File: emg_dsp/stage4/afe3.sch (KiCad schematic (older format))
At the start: 57 parts, among them U32 8X2X100, U33 JUMP, U34 BAV199, U35 BAV199, U36 BAV199, U37 BAV199, U38 TLE2426, U39 REG101, U40 JUMP, U41 ISL28470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

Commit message: added the active electrode - just an INA, opamp, highpass and two lowpasses.
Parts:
- removed C67, C68, C69, C70, C73: 1uf, 0603, symbol C
- removed C71: 0.1uf, 0603, symbol C
- removed C72: 10nf, 0603, symbol C
- removed R26, R27, R28, R29, R30, R31, R32, R33: 2.2k, 0402, symbol R
- removed U32: 8X2X100, 2x8x100mil, symbol 8X2X100
- removed U33, U40: JUMP, 2x100mil, symbol JUMP
- removed U34, U35, U36, U37: BAV199, SOT-363, symbol BAV199
- removed U38: TLE2426, SOIC-8, symbol TLE2426
- removed U39: REG101, SOIC-8, symbol REG101
- removed U41: ISL28470, QSOP-28, symbol ISL28470
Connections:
- wire segments 217 -> 118
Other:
- note removed: "These diodes are optional"
- note removed: "as the inst. amp has ESD diodes"
- note removed: "if they are placed, need low leakage parts"

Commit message: notes, schematic mods, etc.
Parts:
- removed C143, C74, C75, C76, C78, C80, C81, C82: 4.7uf, 0603, symbol C
- removed C77, C79: 1uf, 0603, symbol C
- removed C83, C85, C86: 0.1uf, 0402, symbol C
- removed R34, R35, R41, R42: 327k, 0402, symbol R
- removed R36, R37, R39, R40: 3.3k, 0402, symbol R
- removed R38: 3.3k, 0603, symbol R
- removed U44: ZR4040-2.5, SOT-23, symbol ZR4040-5.0
- removed U45, U46: ADUM2400, SOICW-16, symbol ADUM2400
- added C? (x2): 22uf, 0805, symbol C
- added C? (x3): 10nf, 0402, symbol C
- added C? (x4): 10uf, 0603, symbol C
- added C? (x6): 1uf, 0402, symbol C
- added C? (x4): 1.5nf, 0402, symbol C
- added C? (x5): 2.2uf, 0402, symbol C
- added R? (x4): 1k, 0402, symbol R
- added R? (x5): 100k, 0402, symbol R
- added TP?: CH0, TP, symbol TP
- added TP?: CH1, TP, symbol TP
- added TP?: CH2, TP, symbol TP
- added TP?: CH3, TP, symbol TP
- added U?: MAX253, SOIC-8, symbol MAX253
- added U?: 78250, 78250M, symbol 78250M
- added U? (x6): BAT54S, SOT-23, symbol BAT54
- added U?: TPS78825, SOT-23-5, symbol TPS73025
- added U?: TPS72325, SOT-23-5, symbol TPS72301
- added U?: OPA4348, TSSOP-14, symbol OPA4348
- added U?: LP2985-50, SOT-23-5, symbol TPS73025
- added U? (x3): OPA4348, symbol OPA4348
- added U? (x2): IL715-3, SOIC-16, symbol ADUM2400
- D8: footprint SOD-323 -> SOD-523
- D9: value UCLAMP33 -> SOD-523
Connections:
- net labels added: AV+, AV-, AV0, AV5+, DIN, DOUT, V0, V5, _Enable
- net labels removed: AGnd, AVdd, Din, Dout, IN+A, IN+B, IN+C, IN+D, IN-A, IN-B, IN-C, IN-D, Vdd2
- wire segments 118 -> 173
- no-connect marks 0 -> 6
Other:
- note removed: "battery"
- note removed: "e.g. 4x AAA (6V)"
- note removed: "for loop stability"
- note removed: "may have to short the cap"
- note removed: "need to check this segment"
- moved on the sheet: C144, C84, D8, D9, L8, U42, U43

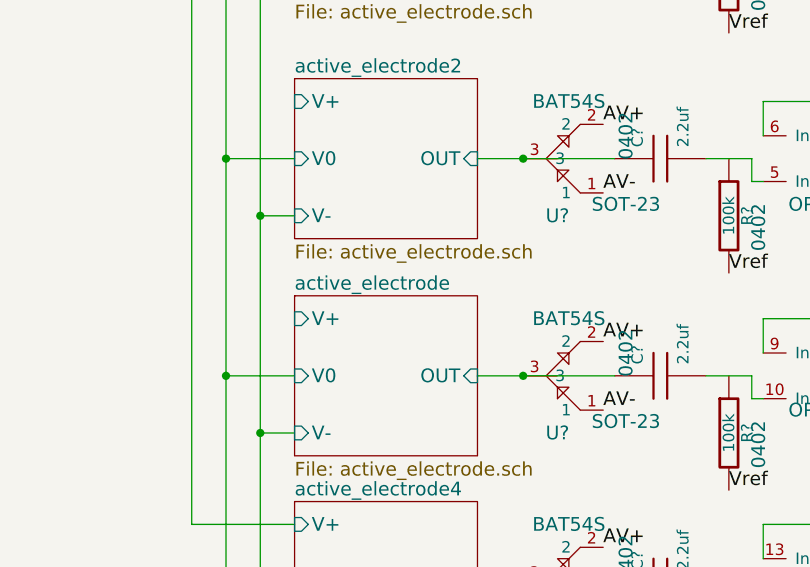
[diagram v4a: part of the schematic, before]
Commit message: revamping the neural AFE
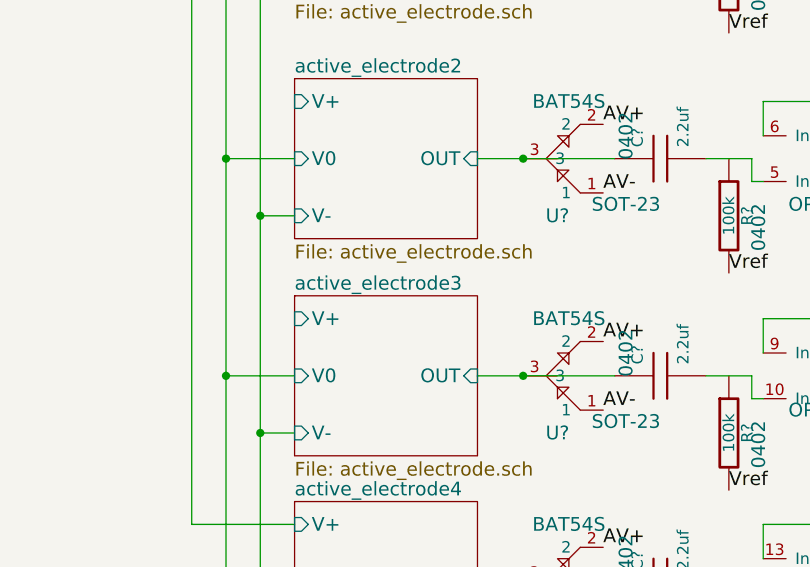
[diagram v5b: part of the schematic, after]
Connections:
- net active_electrode/OUT renamed active_electrode3/OUT
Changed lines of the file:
@@
-EESchema Schematic File Version 2  date Sun 31 Jan 2010 07:35:14 PM EST
+EESchema Schematic File Version 2  date Mon 01 Feb 2010 06:40:42 PM EST
 LIBS:power,device,emg_sym,./stage4.cache
 EELAYER 24  0
@@
 S 2550 3100 800  700
 U 4B6079F1
-F0 "active_electrode" 60
+F0 "active_electrode3" 60
 F1 "active_electrode.sch" 60
 F2 "OUT" I R 3350 3450 60

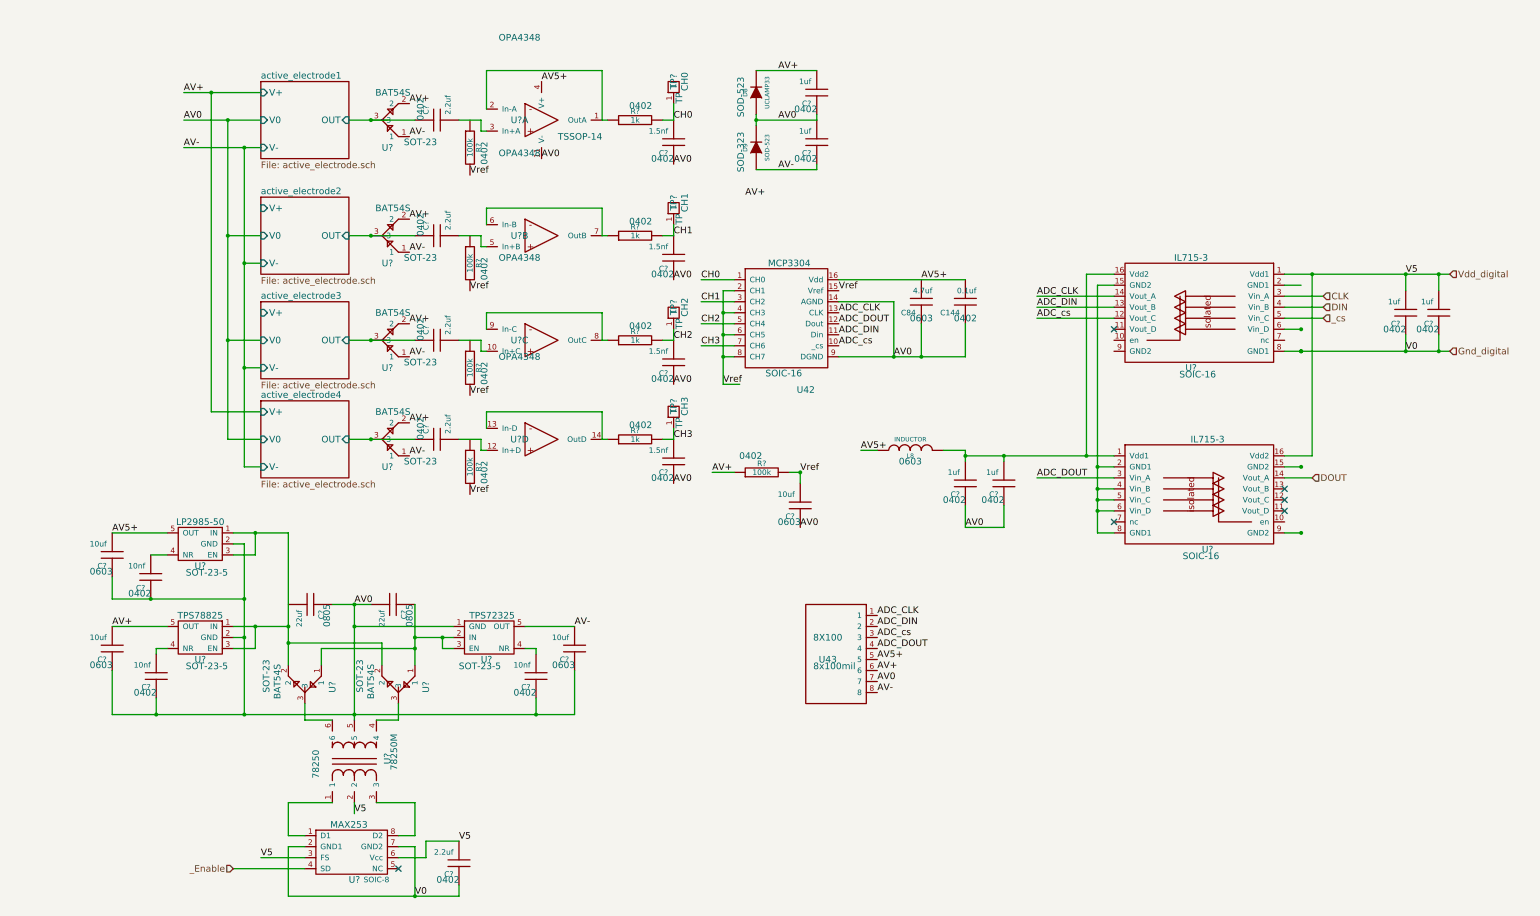
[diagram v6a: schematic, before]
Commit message: getting closer to finalizing the schematic ... added another voltage, beh.
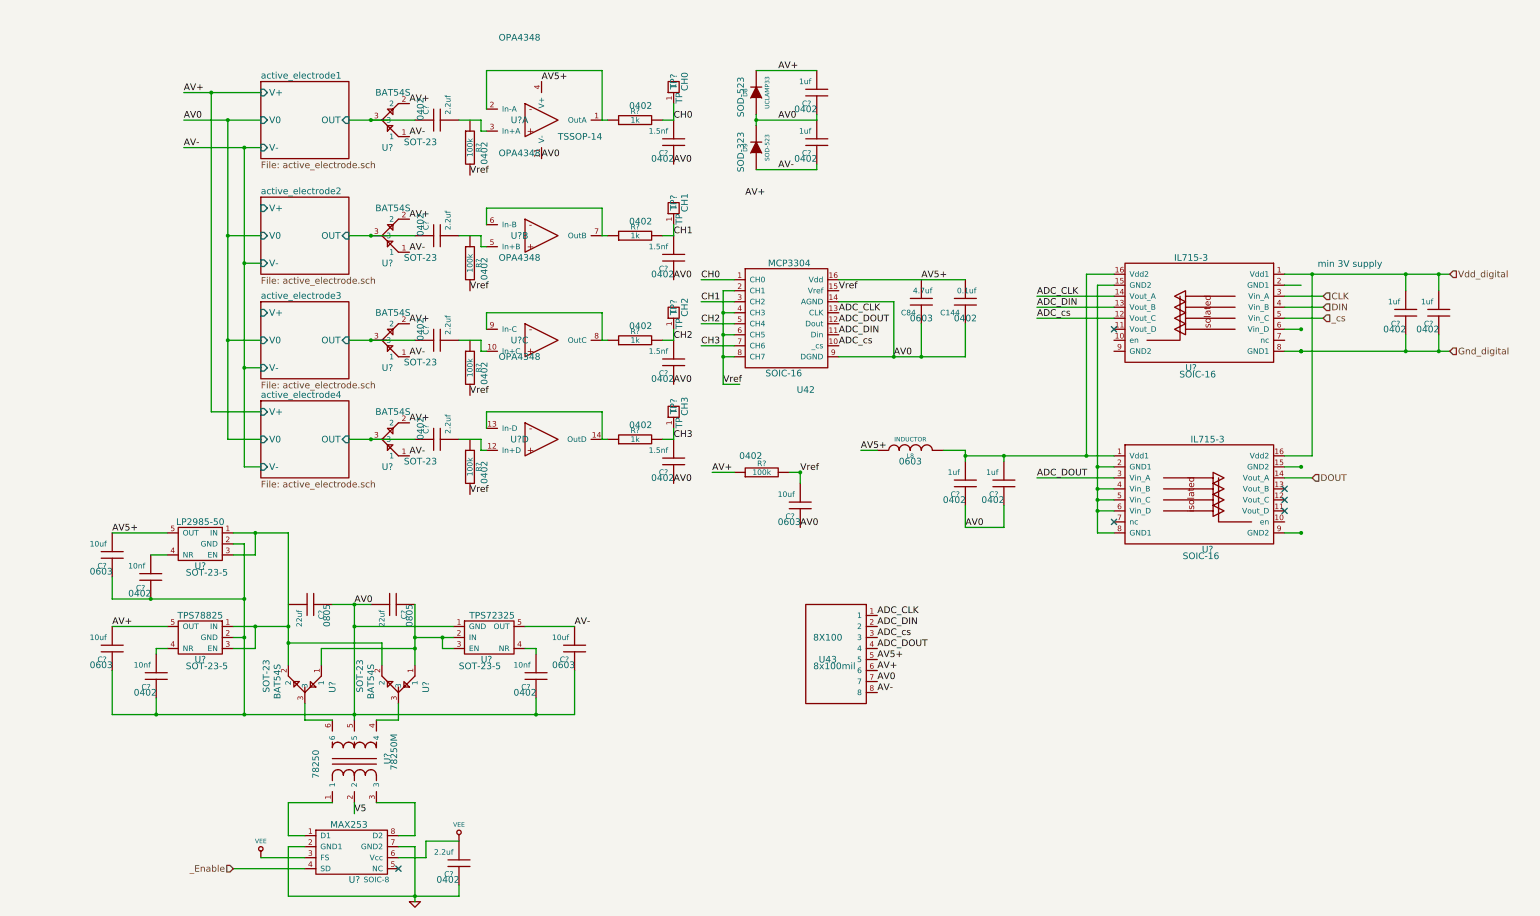
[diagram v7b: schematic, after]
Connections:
- net Gnd_digital: no longer C?.1, U?.2 (GND1), U?.7 (GND2)
- net Vdd_digital: no longer C?.2, U?.2, U?.3 (FS), U?.6 (Vcc)
- new net GND: C?.1, U?.2 (GND1), U?.7 (GND2)
- new net V5: U?.2
- new net VEE: C?.2, U?.3 (FS), U?.6 (Vcc)
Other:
- note added: "min 3V supply"

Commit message: fixing the schematic with the help of the BOM.. trying to make the BOM simpler (and also making sure that U can actually buy all the parts on the board!)
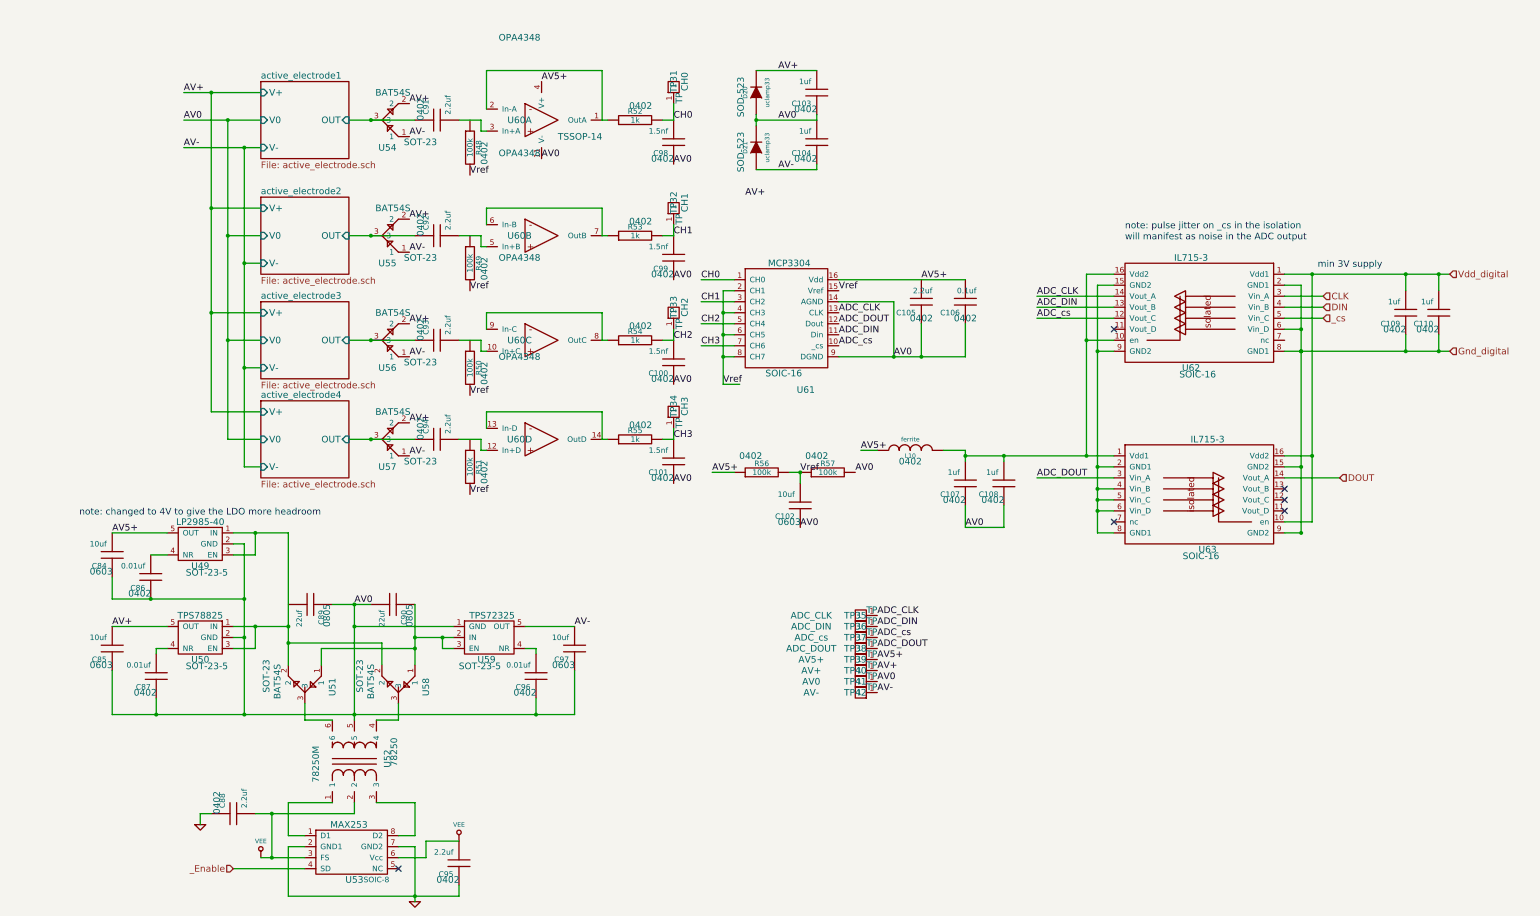
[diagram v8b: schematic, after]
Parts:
- removed U43: 8X100, 8x100mil, symbol 8X100
- added C88: 2.2uf, 0402, symbol C
- added R57: 100k, 0402, symbol R
- added TP35: ADC_CLK, TP, symbol TP
- added TP36: ADC_DIN, TP, symbol TP
- added TP37: ADC_cs, TP, symbol TP
- added TP38: ADC_DOUT, TP, symbol TP
- added TP39: AV5+, TP, symbol TP
- added TP40: AV+, TP, symbol TP
- added TP41: AV0, TP, symbol TP
- added TP42: AV-, TP, symbol TP
- C105: renamed from C84; value 4.7uf -> 2.2uf; footprint 0603 -> 0402
- C86, C87, C96: renamed from C?; value 10nf -> 0.01uf
- D20: renamed from D8; value UCLAMP33 -> uclamp33
- D21: renamed from D9; value SOD-523 -> uclamp33; footprint SOD-323 -> SOD-523
- L10: renamed from L8; value INDUCTOR -> ferrite; footprint 0603 -> 0402
- U49: renamed from U?; value LP2985-50 -> LP2985-40
- U52: renamed from U?; value 78250 -> 78250M; footprint 78250M -> 78250
- U60: renamed from U?; footprint (none) -> TSSOP-14
- gave numbers to parts that had none: 46
- renumbered C144 to C106, U42 to U61
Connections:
- net V5 is gone; now on net VEE: U52.2
- net ADC_CLK: now also TP35.1
- net ADC_DIN: now also TP36.1
- net ADC_DOUT: now also TP38.1
- net ADC_cs: now also TP37.1
- net AV+: now also TP40.1; no longer R56.1
- net AV-: now also TP42.1
- net AV0: now also R57.2, TP41.1
- net AV5+: now also R56.1, TP39.1
- net GND: now also C88.1
- net Gnd_digital: now also U62.2 (GND1), U62.6 (Vin_D), U63.15 (GND2), U63.9 (GND2)
- net VEE: now also C88.2
- net Vdd_digital: now also U63.10 (en)
- net Vref: now also R57.1
- net at C107.2, C108.2, L10.2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: now also U62.10 (en)
- net at U62.15 (GND2), U63.2 (GND1), U63.4 (Vin_B)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: now also U62.9 (GND2)
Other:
- note added: "note: changed to 4V to give the LDO more headroom"
- note added: "note: pulse jitter on _cs in the isolation"
- note added: "will manifest as noise in the ADC output"
